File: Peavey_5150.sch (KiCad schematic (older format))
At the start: 203 parts, among them J165 SEND, J166 RETURN, J2 Power, J3 OUTPUT, J37 INPUT FRONT, J39 INPUT REAR, J4 SWIM, J5 FOOTSWITCH, K1 G5V-2, K2 G5V-2, K3 G5V-2, K4 G5V-2, K5 G5V1, Q1 IRF840, Q2 BC847, Q3 BC847, Q4 BC847, SW2 Clean, SW3 Bright, SW4 FX_loop, U1 MP4462, U2 AMS1117-3.3, U3 STM8S003F3P, U4 TLP222A

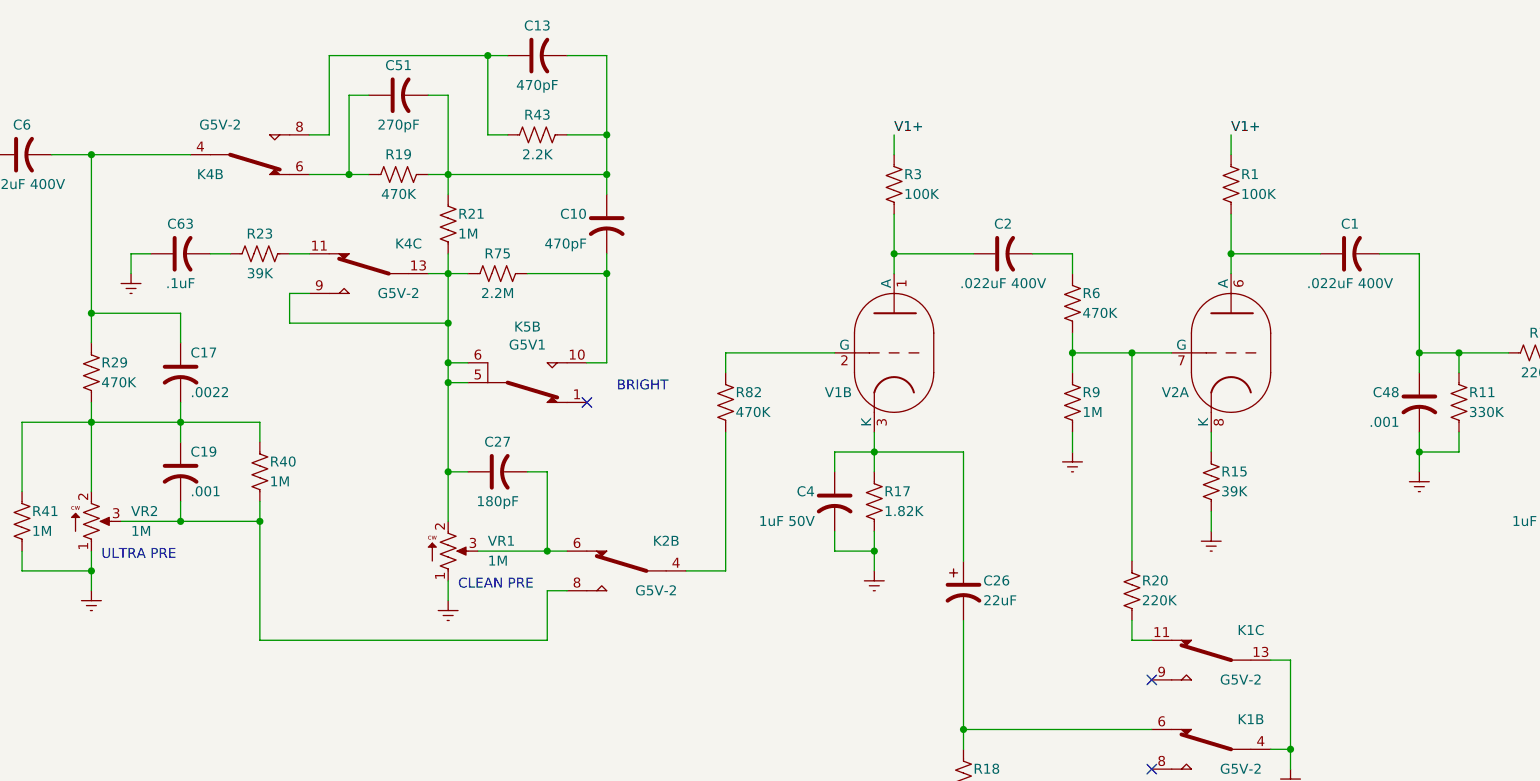
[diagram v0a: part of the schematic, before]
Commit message: add schematic
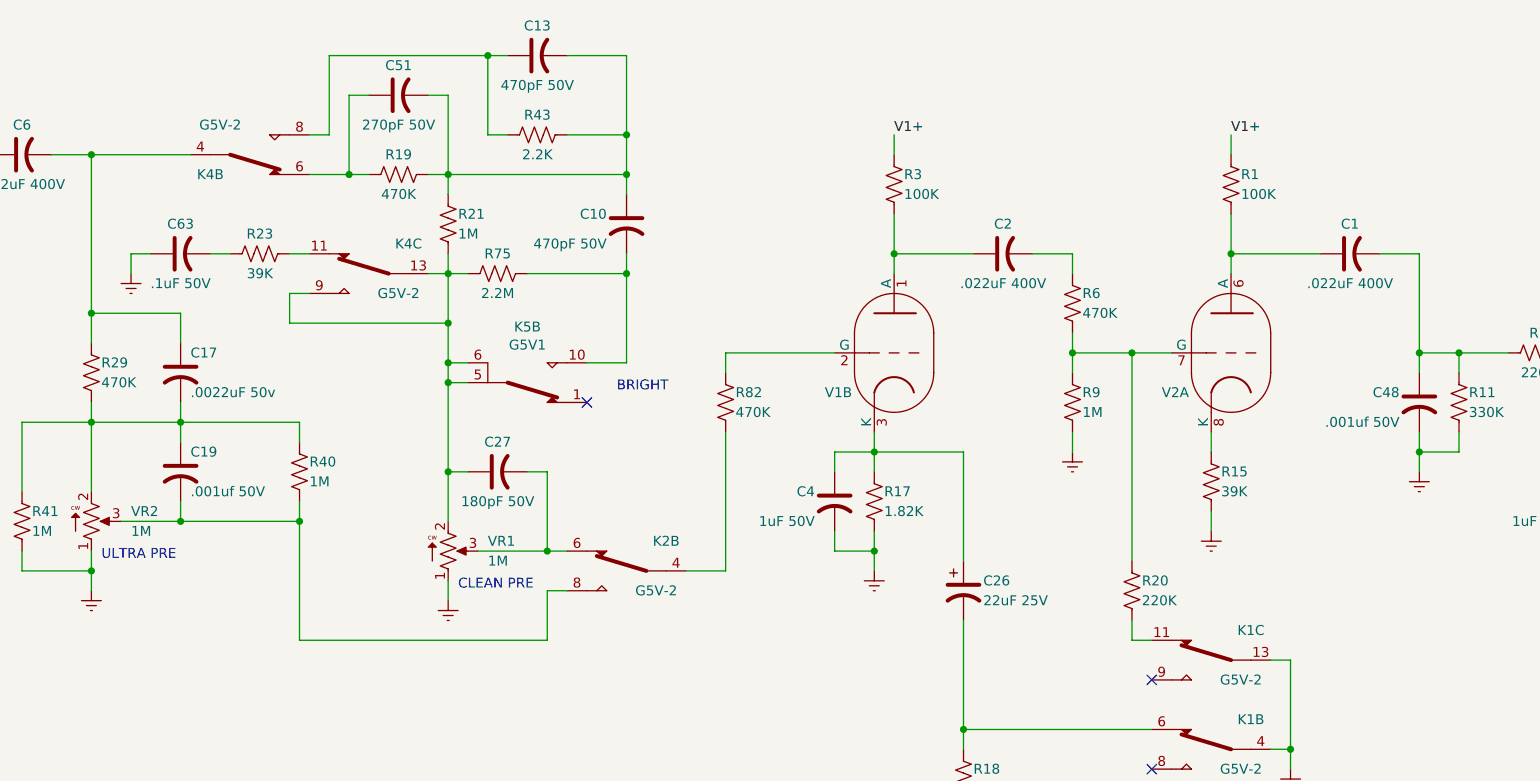
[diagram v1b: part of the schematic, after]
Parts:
- C10, C13: value 470pF -> 470pF 50V
- C17: value .0022 -> .0022uF 50v
- C19, C48: value .001 -> .001uf 50V
- C26: value 22uF -> 22uF 25V
- C27: value 180pF -> 180pF 50V
- C51: value 270pF -> 270pF 50V
- C63: value .1uF -> .1uF 50V
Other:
- moved on the sheet: C10, R40
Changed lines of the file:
@@
 Connection ~ 27650 4950
 Wire Wire Line
-	7850 2600 7850 2500
-Wire Wire Line
-	7850 1900 7850 1500
-Connection ~ 7850 1900
-Connection ~ 7850 2100
-Wire Wire Line
-	7850 2100 7850 1900
-Wire Wire Line
-	7850 2100 7850 2200
-Connection ~ 6100 3850
+	7950 2600 7950 2500
+Wire Wire Line
+	7950 1900 7950 1500
+Connection ~ 7950 1900
+Connection ~ 7950 2100
+Wire Wire Line
+	7950 2100 7950 1900
+Wire Wire Line
+	7950 2100 7950 2200
+Connection ~ 6300 3850
 Wire Wire Line
 	7550 4200 7650 4200
@@
 	7550 4450 7550 4200
 Wire Wire Line
-	6100 4450 7550 4450
-Wire Wire Line
-	6100 3850 6100 4450
+	6300 4450 7550 4450
+Wire Wire Line
+	6300 3850 6300 4450
 Wire Wire Line
 	5250 4100 5250 4000
@@
 Connection ~ 5700 3850
 Wire Wire Line
-	6100 3750 6100 3850
-Wire Wire Line
-	6100 3850 5700 3850
+	6300 3750 6300 3850
+Wire Wire Line
+	6300 3850 5700 3850
 Wire Wire Line
 	5700 3850 5400 3850
@@
 	5250 3350 5250 3250
 Wire Wire Line
-	6100 3350 5700 3350
-Wire Wire Line
-	6100 3450 6100 3350
+	6300 3350 5700 3350
+Wire Wire Line
+	6300 3450 6300 3350
 $Comp
 L Device:R_US R40
 U 1 1 6243533A
-P 6100 3600
-F 0 "R40" H 6050 3550 50  0000 R CNN
-F 1 "1M" H 6050 3650 50  0000 R CNN
-F 2 "" V 6140 3590 50  0001 C CNN
-F 3 "~" H 6100 3600 50  0001 C CNN
-	1    6100 3600
+P 6300 3600
+F 0 "R40" H 6250 3550 50  0000 R CNN
+F 1 "1M" H 6250 3650 50  0000 R CNN
+F 2 "" V 6340 3590 50  0001 C CNN
+F 3 "~" H 6300 3600 50  0001 C CNN
+	1    6300 3600
 	-1   0    0    1
 $EndComp
@@
 P 5700 3600
 F 0 "C19" H 5750 3700 50  0000 L CNN
-F 1 ".001" H 5750 3500 50  0000 L CNN
+F 1 ".001uf 50V" H 5750 3500 50  0000 L CNN
 F 2 "" H 5700 3600 50  0001 C CNN
 F 3 "" H 5700 3600 50  0001 C CNN
@@
 P 5700 3100
 F 0 "C17" H 5750 3200 50  0000 L CNN
-F 1 ".0022" H 5750 3000 50  0000 L CNN
+F 1 ".0022uF 50v" H 5750 3000 50  0000 L CNN
 F 2 "" H 5700 3100 50  0001 C CNN
 F 3 "" H 5700 3100 50  0001 C CNN
@@
 P 7300 3600
 F 0 "C27" V 7450 3600 50  0000 C CNN
-F 1 "180pF" V 7150 3600 50  0000 C CNN
+F 1 "180pF 50V" V 7150 3600 50  0000 C CNN
 F 2 "" H 7300 3600 50  0001 C CNN
 F 3 "" H 7300 3600 50  0001 C CNN
@@
 NoConn ~ 7750 3250
 Wire Wire Line
-	7450 2600 7850 2600
+	7450 2600 7950 2600
 Wire Wire Line
 	7150 2600 7050 2600
@@
 	6350 1900 6450 1900
 Wire Wire Line
-	7650 1900 7850 1900
-Wire Wire Line
-	7850 1500 7650 1500
+	7650 1900 7950 1900
+Wire Wire Line
+	7950 1500 7650 1500
 $Comp
 L Peavey_5150-rescue:C_US-simple-Peavey_5150-rescue C13
@@
 P 7500 1500
 F 0 "C13" V 7650 1500 50  0000 C CNN
-F 1 "470pF" V 7350 1500 50  0000 C CNN
+F 1 "470pF 50V" V 7350 1500 50  0000 C CNN
 F 2 "" H 7500 1500 50  0001 C CNN
 F 3 "" H 7500 1500 50  0001 C CNN
@@
 $EndComp
 Wire Wire Line
-	7050 2100 7850 2100
+	7050 2100 7950 2100
 $Comp
 L Peavey_5150-rescue:C_US-simple-Peavey_5150-rescue C10
 U 1 1 60EB3129
-P 7850 2350
-F 0 "C10" H 7750 2400 50  0000 R CNN
-F 1 "470pF" H 7750 2250 50  0000 R CNN
-F 2 "" H 7850 2350 50  0001 C CNN
-F 3 "" H 7850 2350 50  0001 C CNN
-	1    7850 2350
+P 7950 2350
+F 0 "C10" H 7850 2400 50  0000 R CNN
+F 1 "470pF 50V" H 7850 2250 50  0000 R CNN
+F 2 "" H 7950 2350 50  0001 C CNN
+F 3 "" H 7950 2350 50  0001 C CNN
+	1    7950 2350
 	1    0    0    -1
 $EndComp
@@
 P 5700 2500
 F 0 "C63" V 5850 2500 50  0000 C CNN
-F 1 ".1uF" V 5550 2500 50  0000 C CNN
+F 1 ".1uF 50V" V 5550 2500 50  0000 C CNN
 F 2 "" H 5700 2500 50  0001 C CNN
 F 3 "" H 5700 2500 50  0001 C CNN
@@
 P 6800 1700
 F 0 "C51" V 6950 1700 50  0000 C CNN
-F 1 "270pF" V 6650 1700 50  0000 C CNN
+F 1 "270pF 50V" V 6650 1700 50  0000 C CNN
 F 2 "" H 6800 1700 50  0001 C CNN
 F 3 "" H 6800 1700 50  0001 C CNN
@@
 P 9650 4200
 F 0 "C26" H 9750 4250 50  0000 L CNN
-F 1 "22uF" H 9750 4150 50  0000 L CNN
+F 1 "22uF 25V" H 9750 4150 50  0000 L CNN
 F 2 "Capacitor_THT:CP_Radial_D13.0mm_P5.00mm" H 9650 4200 50  0001 C CNN
 F 3 "~" H 9650 4200 50  0001 C CNN
@@
 P 11950 3250
 F 0 "C48" H 11850 3300 50  0000 R CNN
-F 1 ".001" H 11850 3150 50  0000 R CNN
+F 1 ".001uf 50V" H 11850 3150 50  0000 R CNN
 F 2 "" H 11950 3250 50  0001 C CNN
 F 3 "" H 11950 3250 50  0001 C CNN
@@
 	7050 2850 7050 3050
 Wire Wire Line
-	7750 3050 7850 3050
-Wire Wire Line
-	7850 3050 7850 2600
-Connection ~ 7850 2600
+	7750 3050 7950 3050
+Wire Wire Line
+	7950 3050 7950 2600
+Connection ~ 7950 2600
 Wire Wire Line
 	7150 3050 7050 3050

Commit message: add some r watts
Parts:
- R13, R17: value 1.82K -> 1.82K 1/4W
- R29: value 470K -> 470K 1/4W
- R41: value 1M -> 1M 1/4W
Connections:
- wire segments 724 -> 723
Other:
- moved on the sheet: C15, C19, C20, C3, C6, J37, J39, R12, R2, R22, R25, R29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

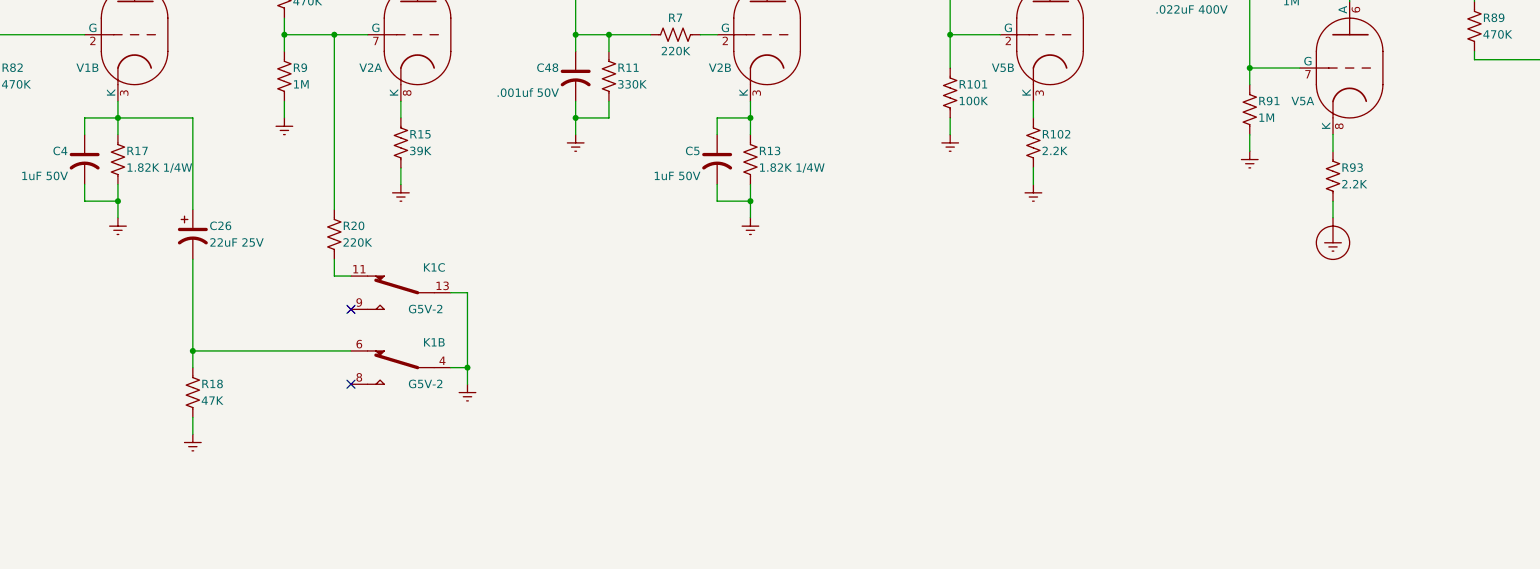
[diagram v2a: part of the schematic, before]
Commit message: add watts to R
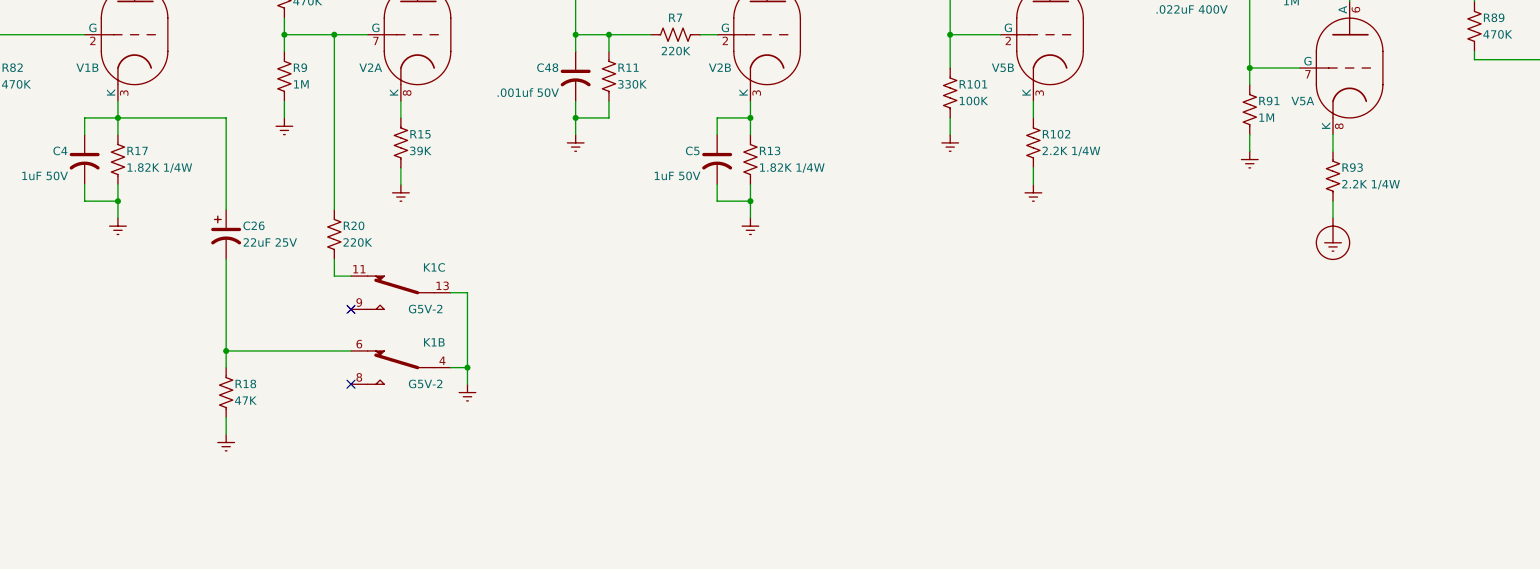
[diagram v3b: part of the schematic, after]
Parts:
- R102, R93: value 2.2K -> 2.2K 1/4W
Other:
- moved on the sheet: C26, R18
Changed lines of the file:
@@
 L Device:CP1 C26
 U 1 1 64D15CF4
-P 9650 4200
-F 0 "C26" H 9750 4250 50  0000 L CNN
-F 1 "22uF 25V" H 9750 4150 50  0000 L CNN
-F 2 "Capacitor_THT:CP_Radial_D13.0mm_P5.00mm" H 9650 4200 50  0001 C CNN
-F 3 "~" H 9650 4200 50  0001 C CNN
-F 4 "VZH152M1VTR-1816" H 9650 4200 50  0001 C CNN "PN"
-	1    9650 4200
-	1    0    0    -1
-$EndComp
-Wire Wire Line
-	9200 3500 9650 3500
-Wire Wire Line
-	9650 3500 9650 4050
-Wire Wire Line
-	10600 4900 9650 4900
-Wire Wire Line
-	9650 4900 9650 4350
+P 9850 4200
+F 0 "C26" H 9950 4250 50  0000 L CNN
+F 1 "22uF 25V" H 9950 4150 50  0000 L CNN
+F 2 "Capacitor_THT:CP_Radial_D13.0mm_P5.00mm" H 9850 4200 50  0001 C CNN
+F 3 "~" H 9850 4200 50  0001 C CNN
+F 4 "VZH152M1VTR-1816" H 9850 4200 50  0001 C CNN "PN"
+	1    9850 4200
+	1    0    0    -1
+$EndComp
+Wire Wire Line
+	9200 3500 9850 3500
+Wire Wire Line
+	9850 3500 9850 4050
+Wire Wire Line
+	10600 4900 9850 4900
+Wire Wire Line
+	9850 4900 9850 4350
 $Comp
 L Device:R_US R18
 U 1 1 650568DF
-P 9650 5150
-F 0 "R18" H 9600 5100 50  0000 R CNN
-F 1 "47K" H 9600 5200 50  0000 R CNN
-F 2 "" V 9690 5140 50  0001 C CNN
-F 3 "~" H 9650 5150 50  0001 C CNN
-	1    9650 5150
+P 9850 5150
+F 0 "R18" H 9800 5100 50  0000 R CNN
+F 1 "47K" H 9800 5200 50  0000 R CNN
+F 2 "" V 9890 5140 50  0001 C CNN
+F 3 "~" H 9850 5150 50  0001 C CNN
+	1    9850 5150
 	-1   0    0    1
 $EndComp
@@
 L power:Earth #PWR0123
 U 1 1 6505764E
-P 9650 5400
-F 0 "#PWR0123" H 9650 5150 50  0001 C CNN
-F 1 "Earth" H 9650 5250 50  0001 C CNN
-F 2 "" H 9650 5400 50  0001 C CNN
-F 3 "~" H 9650 5400 50  0001 C CNN
-	1    9650 5400
-	1    0    0    -1
-$EndComp
-Wire Wire Line
-	9650 5400 9650 5300
-Wire Wire Line
-	9650 5000 9650 4900
-Connection ~ 9650 4900
+P 9850 5400
+F 0 "#PWR0123" H 9850 5150 50  0001 C CNN
+F 1 "Earth" H 9850 5250 50  0001 C CNN
+F 2 "" H 9850 5400 50  0001 C CNN
+F 3 "~" H 9850 5400 50  0001 C CNN
+	1    9850 5400
+	1    0    0    -1
+$EndComp
+Wire Wire Line
+	9850 5400 9850 5300
+Wire Wire Line
+	9850 5000 9850 4900
+Connection ~ 9850 4900
 $Comp
 L Device:R_US R1
@@
 P 14700 3650
 F 0 "R102" H 14650 3600 50  0000 R CNN
-F 1 "2.2K" H 14650 3700 50  0000 R CNN
+F 1 "2.2K 1/4W" H 14650 3700 50  0000 R CNN
 F 2 "" V 14740 3640 50  0001 C CNN
 F 3 "~" H 14700 3650 50  0001 C CNN
@@
 P 16500 3850
 F 0 "R93" H 16450 3800 50  0000 R CNN
-F 1 "2.2K" H 16450 3900 50  0000 R CNN
+F 1 "2.2K 1/4W" H 16450 3900 50  0000 R CNN
 F 2 "" V 16540 3840 50  0001 C CNN
 F 3 "~" H 16500 3850 50  0001 C CNN
